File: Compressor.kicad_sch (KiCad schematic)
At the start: 9 parts, among them J1 1217127-1, J2 1217127-1, J3 1217127-1, J4 1217127-1, U1 BQ297xy

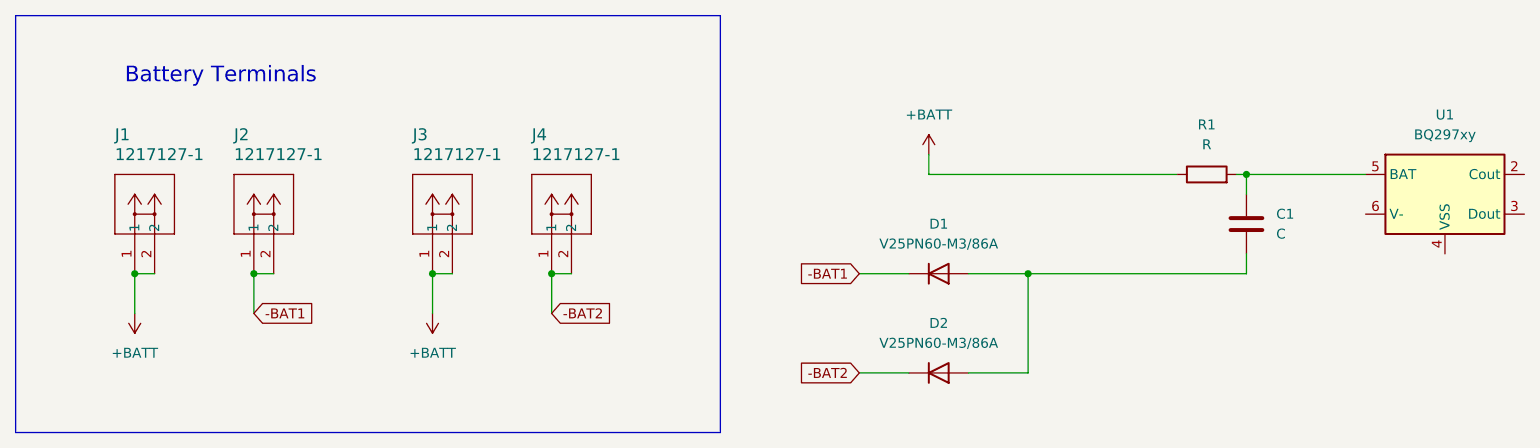
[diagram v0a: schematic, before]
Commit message: Added external power source
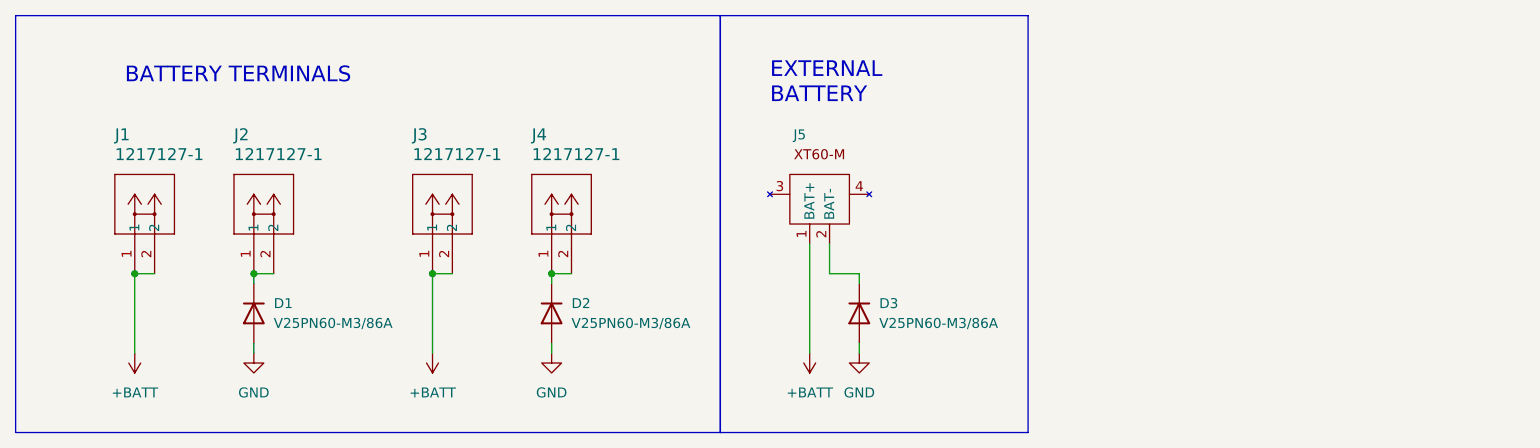
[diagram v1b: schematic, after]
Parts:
- removed C1: C, symbol Device:C
- removed R1: R, symbol Device:R
- removed U1: BQ297xy, Package_SON:WSON-6_1.5x1.5mm_P0.5mm, symbol Battery_Management:BQ297xy
- added D3: V25PN60-M3/86A, Package_TO_SOT_SMD:TO-277A, symbol Diode:VS-6ESU06
- added J5: ~, symbol Compressor:XT60-M-PCB
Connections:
- net +BATT: now also J5.1 (BAT+)
- net GND: now reaches D1.1 (A), D1.2 (A), D2.1 (A), D2.2 (A)
- net GND: now also D3.1 (A), D3.2 (A)
- net -BAT1: no longer names the net of D1.3 (K), J2.1, J2.2
- net -BAT2: no longer names the net of D2.3 (K), J4.1, J4.2
- new net: D3.3 (K), J5.2 (BAT-)
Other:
- note added: "BATTERY TERMINALS"
- note added: "EXTERNAL BATTERY"
- note removed: "Battery Terminals"

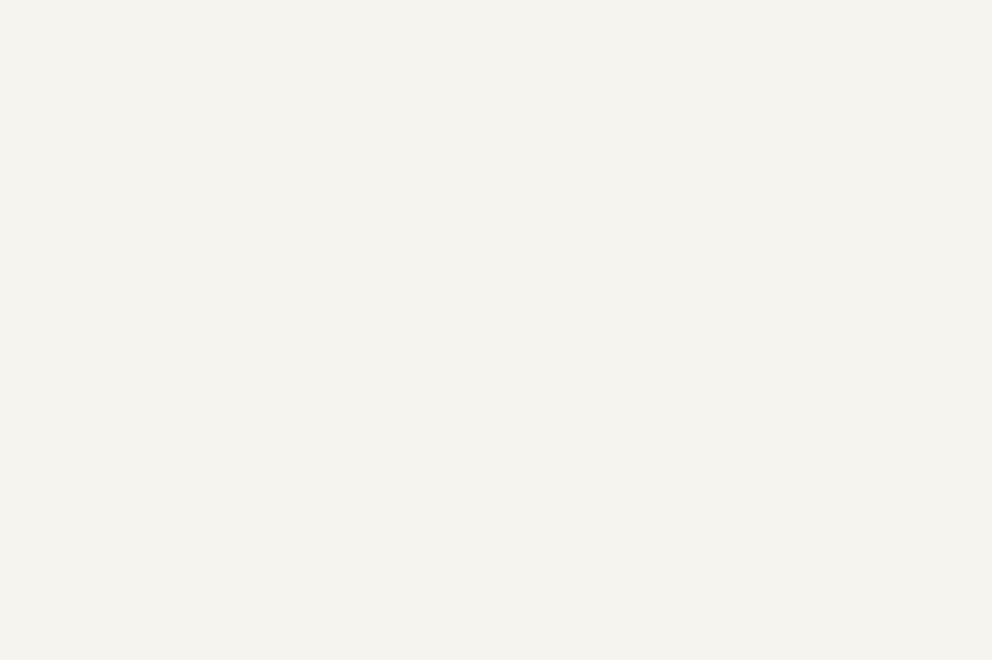
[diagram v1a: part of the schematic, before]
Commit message: Added motor output and driver circuit
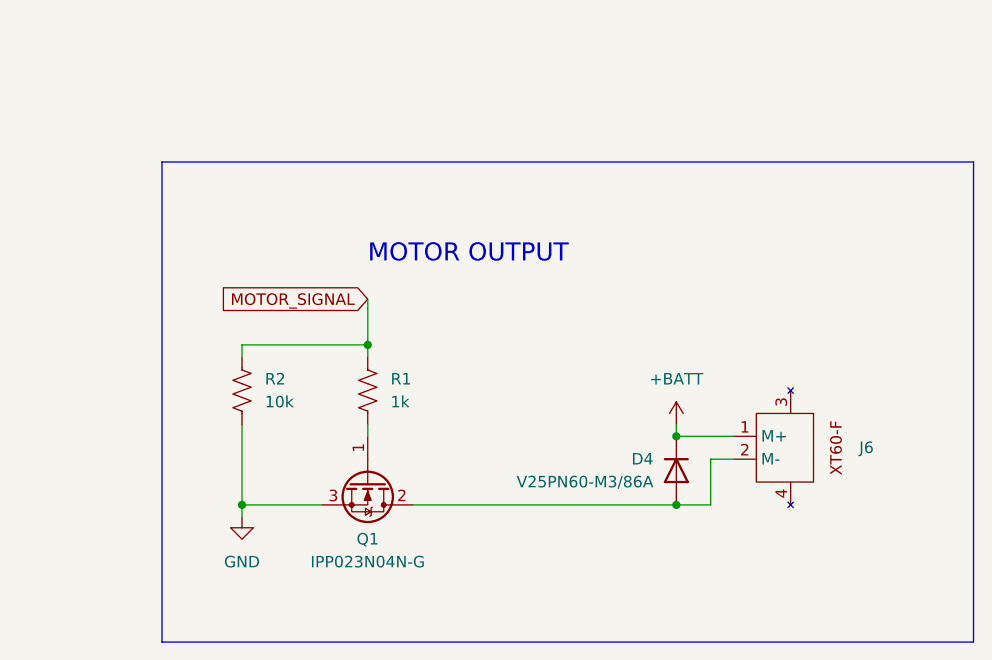
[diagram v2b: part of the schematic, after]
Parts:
- added D4: V25PN60-M3/86A, Package_TO_SOT_SMD:TO-277A, symbol Diode:VS-6ESU06
- added J6: ~, symbol Compressor:XT60-F-PCB
- added Q1: IPP023N04N-G, Package_TO_SOT_THT:TO-220-3_Vertical, symbol Transistor_FET:BUZ11
- added R1: 1k, Resistor_SMD:R_0603_1608Metric, symbol Device:R_US
- added R2: 10k, Resistor_SMD:R_0603_1608Metric, symbol Device:R_US
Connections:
- net +BATT: now also D4.3 (K), J6.1 (M+)
- net GND: now also Q1.3 (S), R2.2
- new net: Q1.1 (G), R1.2
- new net: D4.1 (A), D4.2 (A), J6.2 (M-), Q1.2 (D)
- new net MOTOR_SIGNAL: R1.1, R2.1
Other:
- note added: "MOTOR OUTPUT"
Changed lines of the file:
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@@
   (junction (at 66.04 45.72) (diameter 0) (color 0 0 0 0)
   )
+  (junction (at 203.2 149.86) (diameter 0) (color 0 0 0 0)
+  )
+  (junction (at 251.46 142.24) (diameter 0) (color 0 0 0 0)
+  )
+  (junction (at 251.46 149.86) (diameter 0) (color 0 0 0 0)
+  )
+  (junction (at 217.17 132.08) (diameter 0) (color 0 0 0 0)
+  )
   (junction (at 27.94 45.72) (diameter 0) (color 0 0 0 0)
   )
@@
     (stroke (width 0) (type default))
   )
+  (wire (pts (xy 217.17 132.08) (xy 217.17 133.35))
+    (stroke (width 0) (type default))
+  )
   (wire (pts (xy 43.18 45.72) (xy 45.72 45.72))
     (stroke (width 0) (type default))
   )
+  (wire (pts (xy 212.09 149.86) (xy 203.2 149.86))
+    (stroke (width 0) (type default))
+  )
   (wire (pts (xy 27.94 45.72) (xy 30.48 45.72))
     (stroke (width 0) (type default))
   )
+  (wire (pts (xy 251.46 142.24) (xy 257.81 142.24))
+    (stroke (width 0) (type default))
+  )
   (wire (pts (xy 81.28 54.61) (xy 81.28 55.88))
     (stroke (width 0) (type default))
   )
+  (wire (pts (xy 222.25 149.86) (xy 251.46 149.86))
+    (stroke (width 0) (type default))
+  )
   (wire (pts (xy 116.84 41.91) (xy 116.84 45.72))
     (stroke (width 0) (type default))
@@
     (stroke (width 0) (type default))
   )
+  (wire (pts (xy 203.2 149.86) (xy 203.2 151.13))
+    (stroke (width 0) (type default))
+  )
   (wire (pts (xy 120.65 54.61) (xy 120.65 55.88))
     (stroke (width 0) (type default))
   )
+  (wire (pts (xy 203.2 140.97) (xy 203.2 149.86))
+    (stroke (width 0) (type default))
+  )
+  (wire (pts (xy 255.27 149.86) (xy 255.27 144.78))
+    (stroke (width 0) (type default))
+  )
   (wire (pts (xy 43.18 45.72) (xy 43.18 46.99))
     (stroke (width 0) (type default))
@@
     (stroke (width 0) (type default))
   )
+  (wire (pts (xy 251.46 140.97) (xy 251.46 142.24))
+    (stroke (width 0) (type default))
+  )
   (wire (pts (xy 66.04 45.72) (xy 66.04 55.88))
     (stroke (width 0) (type default))
   )
+  (wire (pts (xy 203.2 132.08) (xy 217.17 132.08))
+    (stroke (width 0) (type default))
+  )
+  (wire (pts (xy 217.17 127) (xy 217.17 132.08))
+    (stroke (width 0) (type default))
+  )
   (wire (pts (xy 116.84 45.72) (xy 120.65 45.72))
     (stroke (width 0) (type default))
   )
+  (wire (pts (xy 217.17 140.97) (xy 217.17 142.24))
+    (stroke (width 0) (type default))
+  )
+  (wire (pts (xy 255.27 144.78) (xy 257.81 144.78))
+    (stroke (width 0) (type default))
+  )
+  (wire (pts (xy 251.46 149.86) (xy 255.27 149.86))
+    (stroke (width 0) (type default))
+  )
+  (wire (pts (xy 203.2 133.35) (xy 203.2 132.08))
+    (stroke (width 0) (type default))
+  )
   (rectangle (start 102.87 12.7) (end 142.24 66.04)
     (stroke (width 0) (type default))
     (fill (type none))
   )
+  (rectangle (start 194.31 111.76) (end 284.48 165.1)
+    (stroke (width 0) (type default))
+    (fill (type none))
+  )
   (rectangle (start 12.7 12.7) (end 102.87 66.04)
     (stroke (width 0) (type default))
     (fill (type none))
+  )
+  (text "MOTOR OUTPUT" (at 217.17 123.19 0)
+    (effects (font (size 2 2)) (justify left bottom))
   )
   (text "EXTERNAL\nBATTERY" (at 109.22 24.13 0)
@@
     (effects (font (size 2 2)) (justify left bottom))
   )
+  (global_label "MOTOR_SIGNAL" (shape input) (at 217.17 127 180) (fields_autoplaced)
+    (effects (font (size 1.27 1.27)) (justify right))
+    (property "Intersheetrefs" "${INTERSHEET_REFS}" (at 200.3357 127 0)
+      (effects (font (size 1.27 1.27)) (justify right) hide)
+    )
+  )
+  (symbol (lib_id "Device:R_US") (at 217.17 137.16 0) (unit 1)
+    (in_bom yes) (on_board yes) (dnp no) (fields_autoplaced)
+    (property "Reference" "R1" (at 219.71 135.89 0)
+      (effects (font (size 1.27 1.27)) (justify left))
+    )
+    (property "Value" "1k" (at 219.71 138.43 0)
+      (effects (font (size 1.27 1.27)) (justify left))
+    )
+    (property "Footprint" "Resistor_SMD:R_0603_1608Metric" (at 218.186 137.414 90)
+      (effects (font (size 1.27 1.27)) hide)
+    )
+    (property "Datasheet" "~" (at 217.17 137.16 0)
+      (effects (font (size 1.27 1.27)) hide)
+    )
+    (pin "1")
+    (pin "2")
+    (instances
+      (project "Compressor"
+        (path "/c6ed8307-fe38-4e78-9db7-408ca8ca7c58"
+          (reference "R1") (unit 1)
+        )
+      )
+    )
+  )
   (symbol (lib_id "Diode:VS-6ESU06") (at 43.18 50.8 90) (mirror x) (unit 1)
     (in_bom yes) (on_board yes) (dnp no) (fields_autoplaced)
@@
         (path "/c6ed8307-fe38-4e78-9db7-408ca8ca7c58"
           (reference "#PWR03") (unit 1)
+        )
+      )
+    )
+  )
+  (symbol (lib_id "Compressor:XT60-F-PCB") (at 271.78 140.97 270) (unit 1)
+    (in_bom yes) (on_board yes) (dnp no) (fields_autoplaced)
+    (property "Reference" "J6" (at 271.78 143.51 90)
+      (effects (font (size 1.27 1.27)) (justify left))
+    )
+    (property "Value" "~" (at 271.78 140.97 0)
+      (effects (font (size 1.27 1.27)))
+    )
+    (property "Footprint" "" (at 271.78 140.97 0)
+      (effects (font (size 1.27 1.27)) hide)
+    )
+    (property "Datasheet" "" (at 271.78 140.97 0)
+      (effects (font (size 1.27 1.27)) hide)
+    )
+    (pin "1")
+    (pin "2")
+    (pin "3")
+    (pin "4")
+    (instances
+      (project "Compressor"
+        (path "/c6ed8307-fe38-4e78-9db7-408ca8ca7c58"
+          (reference "J6") (unit 1)
+        )
+      )
+    )
+  )
+  (symbol (lib_id "power:GND") (at 203.2 151.13 0) (unit 1)
+    (in_bom yes) (on_board yes) (dnp no) (fields_autoplaced)
+    (property "Reference" "#PWR08" (at 203.2 157.48 0)
+      (effects (font (size 1.27 1.27)) hide)
+    )
+    (property "Value" "GND" (at 203.2 156.21 0)
+      (effects (font (size 1.27 1.27)))
+    )
+    (property "Footprint" "" (at 203.2 151.13 0)
+      (effects (font (size 1.27 1.27)) hide)
+    )
+    (property "Datasheet" "" (at 203.2 151.13 0)
+      (effects (font (size 1.27 1.27)) hide)
+    )
+    (pin "1")
+    (instances
+      (project "Compressor"
+        (path "/c6ed8307-fe38-4e78-9db7-408ca8ca7c58"
+          (reference "#PWR08") (unit 1)
+        )
+      )
+    )
+  )
+  (symbol (lib_id "Diode:VS-6ESU06") (at 251.46 146.05 270) (unit 1)
+    (in_bom yes) (on_board yes) (dnp no)
+    (property "Reference" "D4" (at 248.92 144.78 90)
+      (effects (font (size 1.27 1.27)) (justify right))
+    )
+    (property "Value" "V25PN60-M3/86A" (at 248.92 147.32 90)
+      (effects (font (size 1.27 1.27)) (justify right))
+    )
+    (property "Footprint" "Package_TO_SOT_SMD:TO-277A" (at 247.015 146.05 0)
+      (effects (font (size 1.27 1.27)) hide)
+    )
+    (property "Datasheet" "https://www.vishay.com/docs/94987/vs-6esu06hm3.pdf" (at 251.46 146.05 0)
+      (effects (font (size 1.27 1.27)) hide)
+    )
+    (pin "1")
+    (pin "2")
+    (pin "3")
+    (instances
+      (project "Compressor"
+        (path "/c6ed8307-fe38-4e78-9db7-408ca8ca7c58"
+          (reference "D4") (unit 1)
         )
       )
@@
     )
   )
+  (symbol (lib_id "Device:R_US") (at 203.2 137.16 0) (unit 1)
+    (in_bom yes) (on_board yes) (dnp no) (fields_autoplaced)
+    (property "Reference" "R2" (at 205.74 135.89 0)
+      (effects (font (size 1.27 1.27)) (justify left))
+    )
+    (property "Value" "10k" (at 205.74 138.43 0)
+      (effects (font (size 1.27 1.27)) (justify left))
+    )
+    (property "Footprint" "Resistor_SMD:R_0603_1608Metric" (at 204.216 137.414 90)
+      (effects (font (size 1.27 1.27)) hide)
+    )
+    (property "Datasheet" "~" (at 203.2 137.16 0)
+      (effects (font (size 1.27 1.27)) hide)
+    )
+    (pin "1")
+    (pin "2")
+    (instances
+      (project "Compressor"
+        (path "/c6ed8307-fe38-4e78-9db7-408ca8ca7c58"
+          (reference "R2") (unit 1)
+        )
+      )
+    )
+  )
   (symbol (lib_id "TE-1217127-SYM:1217861-1") (at 81.28 45.72 90) (unit 1)
     (in_bom yes) (on_board yes) (dnp no)
@@
         )
       )
+    )
+  )
+  (symbol (lib_id "Transistor_FET:BUZ11") (at 217.17 147.32 270) (unit 1)
+    (in_bom yes) (on_board yes) (dnp no) (fields_autoplaced)
+    (property "Reference" "Q1" (at 217.17 153.67 90)
+      (effects (font (size 1.27 1.27)))
+    )
+    (property "Value" "IPP023N04N-G" (at 217.17 156.21 90)
+      (effects (font (size 1.27 1.27)))
+    )
+    (property "Footprint" "Package_TO_SOT_THT:TO-220-3_Vertical" (at 215.265 153.67 0)
+      (effects (font (size 1.27 1.27) italic) (justify left) hide)
+    )
+    (property "Datasheet" "https://media.digikey.com/pdf/Data%20Sheets/Fairchild%20PDFs/BUZ11.pdf" (at 217.17 147.32 0)
+      (effects (font (size 1.27 1.27)) (justify left) hide)
+    )
+    (pin "1")
+    (pin "2")
+    (pin "3")
+    (instances
+      (project "Compressor"
+        (path "/c6ed8307-fe38-4e78-9db7-408ca8ca7c58"
+          (reference "Q1") (unit 1)
+        )
+      )
+    )
+  )
+  (symbol (lib_id "power:+BATT") (at 251.46 140.97 0) (unit 1)
+    (in_bom yes) (on_board yes) (dnp no) (fields_autoplaced)
+    (property "Reference" "#PWR07" (at 251.46 144.78 0)
+      (effects (font (size 1.27 1.27)) hide)
+    )
+    (property "Value" "+BATT" (at 251.46 135.89 0)
+      (effects (font (size 1.27 1.27)))
+    )
+    (property "Footprint" "" (at 251.46 140.97 0)
+      (effects (font (size 1.27 1.27)) hide)
+    )
+    (property "Datasheet" "" (at 251.46 140.97 0)
+      (effects (font (size 1.27 1.27)) hide)
+    )
+    (pin "1")
+    (instances
+      (project "Compressor"
+        (path "/c6ed8307-fe38-4e78-9db7-408ca8ca7c58"
+          (reference "#PWR07") (unit 1)
+        )
+      )
